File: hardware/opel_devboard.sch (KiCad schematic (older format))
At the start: 0 parts

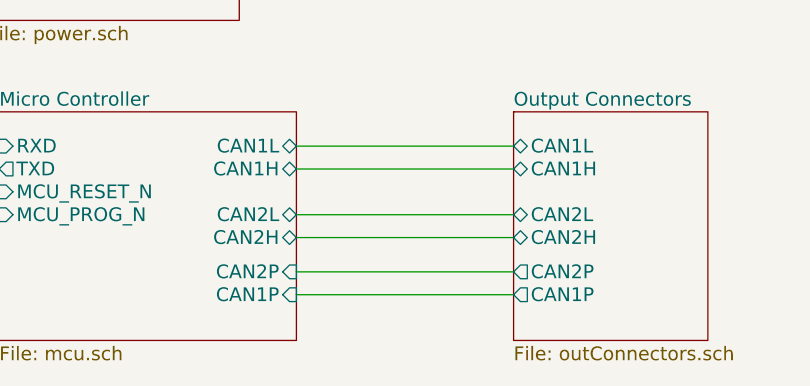
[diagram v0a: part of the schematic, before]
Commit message: Fixed some warnings (like unconnected pins)
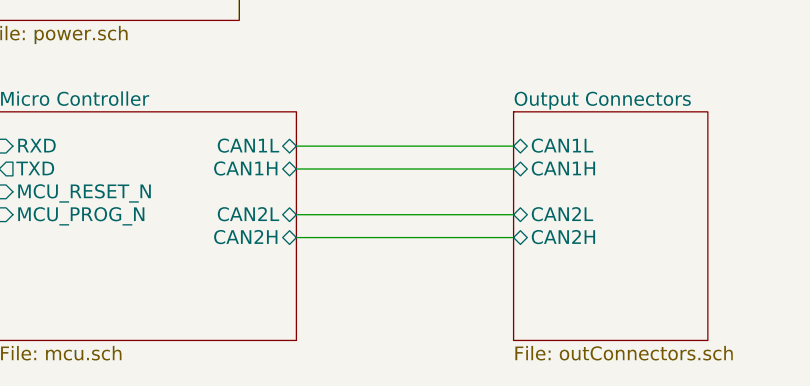
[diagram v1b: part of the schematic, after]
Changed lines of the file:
@@
 F8 "CAN2L" B R 5800 3000 60
 F9 "CAN2H" B R 5800 3100 60
-F10 "CAN2P" I R 5800 3250 60
-F11 "CAN1P" I R 5800 3350 60
 $EndSheet
 $Sheet
@@
 F4 "CAN2H" B L 6750 3100 60
 F5 "CAN2L" B L 6750 3000 60
-F6 "CAN2P" O L 6750 3250 60
-F7 "CAN1P" O L 6750 3350 60
 $EndSheet
 Wire Wire Line
@@
 Wire Wire Line
 	5800 2700 6750 2700
-Wire Wire Line
-	6750 3250 5800 3250
-Wire Wire Line
-	5800 3350 6750 3350
 $Comp
 L +5V #PWR02
